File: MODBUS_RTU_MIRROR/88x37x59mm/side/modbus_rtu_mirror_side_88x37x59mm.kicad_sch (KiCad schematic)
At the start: 5 parts, among them J1 Conn_01x04_Male, J2 Conn_01x04_Male, U1 ESP32-WROOM-32, U2 TXS0108EPW, U3 AMS1117-3.3

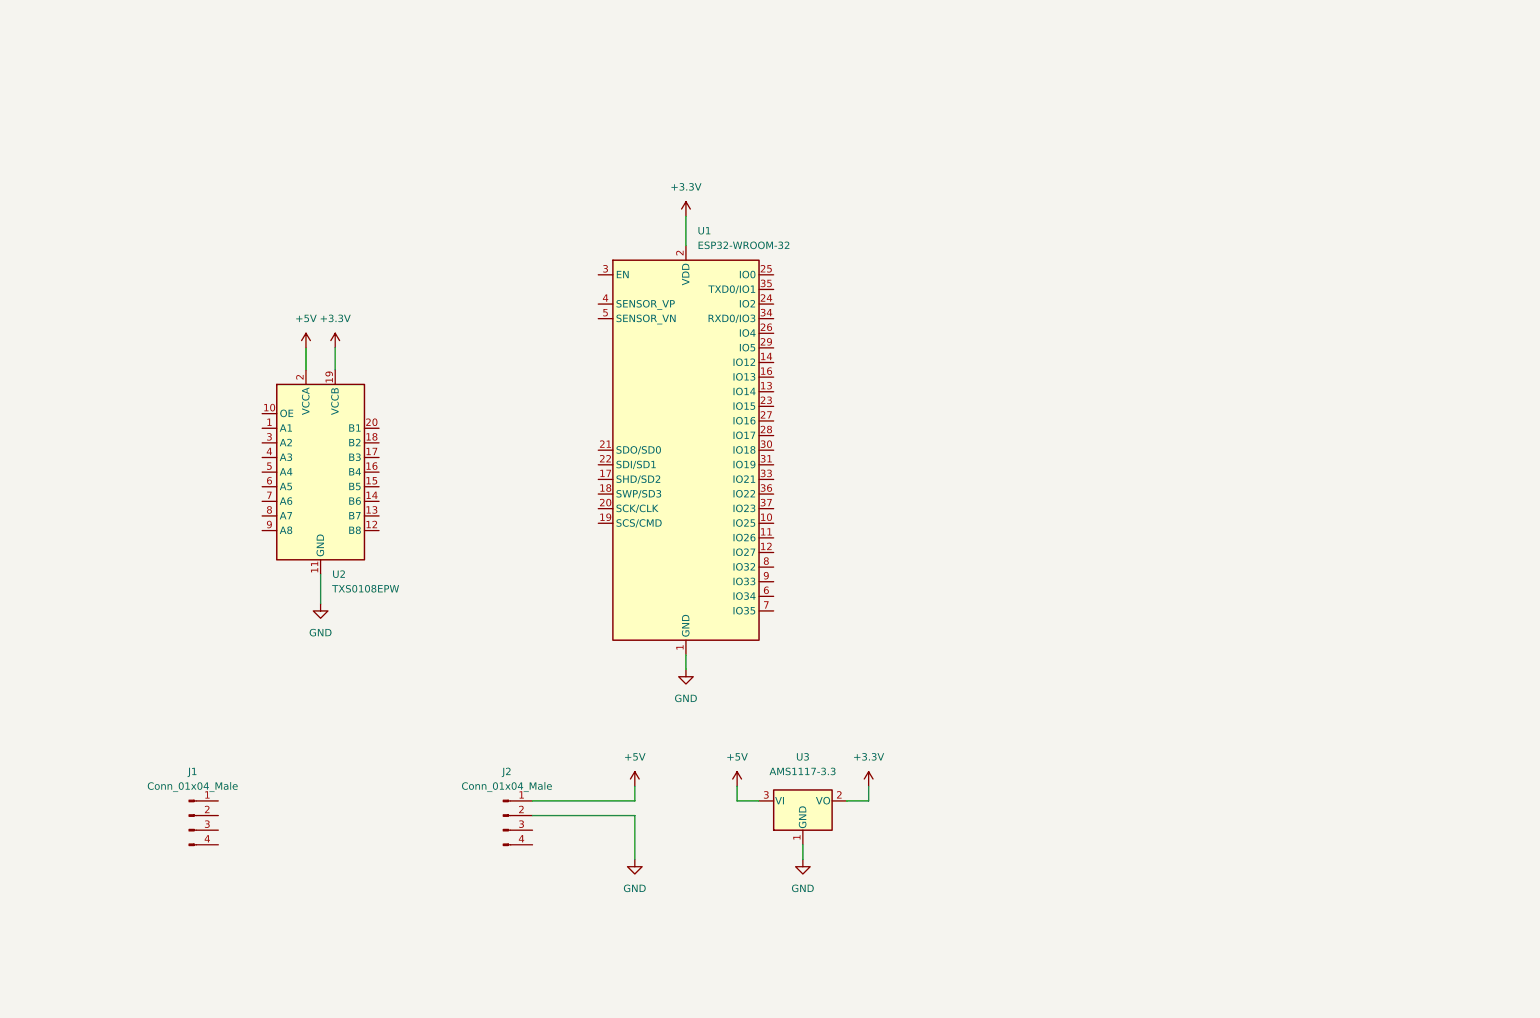
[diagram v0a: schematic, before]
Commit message: added capacitors, rtc, prog header
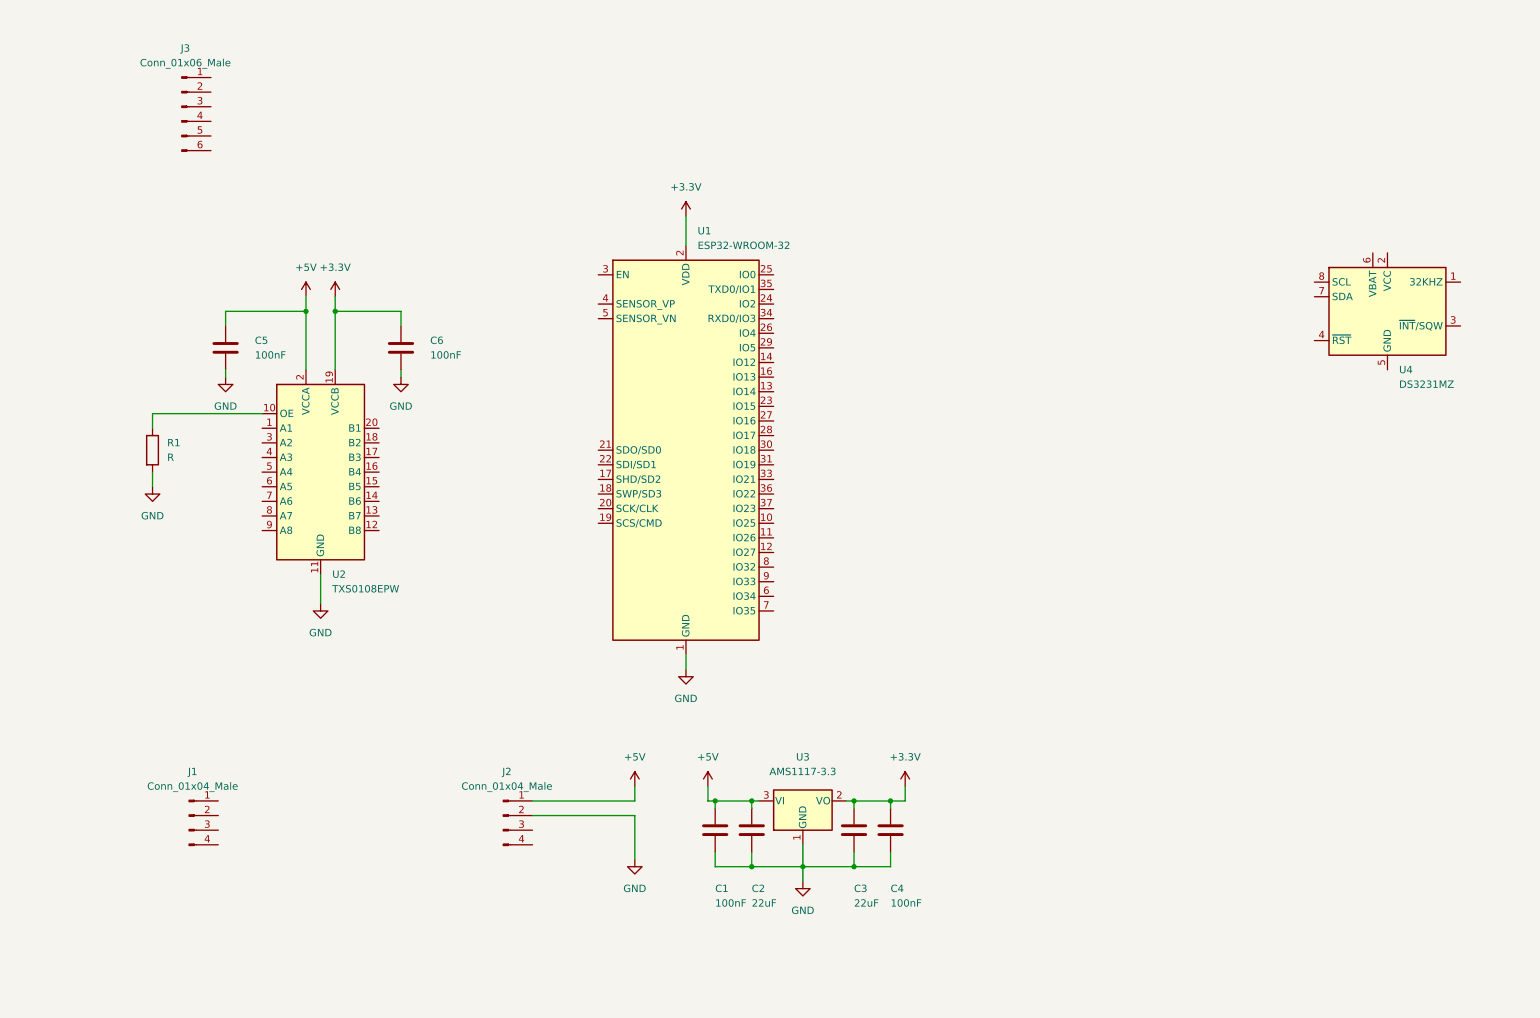
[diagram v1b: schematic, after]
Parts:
- added C1, C4, C5, C6: 100nF, Capacitor_SMD:C_0805_2012Metric_Pad1.18x1.45mm_HandSolder, symbol Device:C
- added C2, C3: 22uF, Capacitor_SMD:C_0805_2012Metric_Pad1.18x1.45mm_HandSolder, symbol Device:C
- added J3: Conn_01x06_Male, Connector_PinHeader_2.54mm:PinHeader_1x06_P2.54mm_Vertical, symbol Connector:Conn_01x06_Male
- added R1: R, Resistor_SMD:R_0805_2012Metric_Pad1.20x1.40mm_HandSolder, symbol Device:R
- added U4: DS3231MZ, Package_SO:SOIC-8_3.9x4.9mm_P1.27mm, symbol Timer_RTC:DS3231MZ
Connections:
- net +3.3V: now also C3.1, C4.1, C6.1
- net +5V: now also C1.1, C2.1, C5.1
- net GND: now also C1.2, C2.2, C3.2, C4.2, C5.2, C6.2, R1.2
- net at U2.10 (OE): now also R1.1

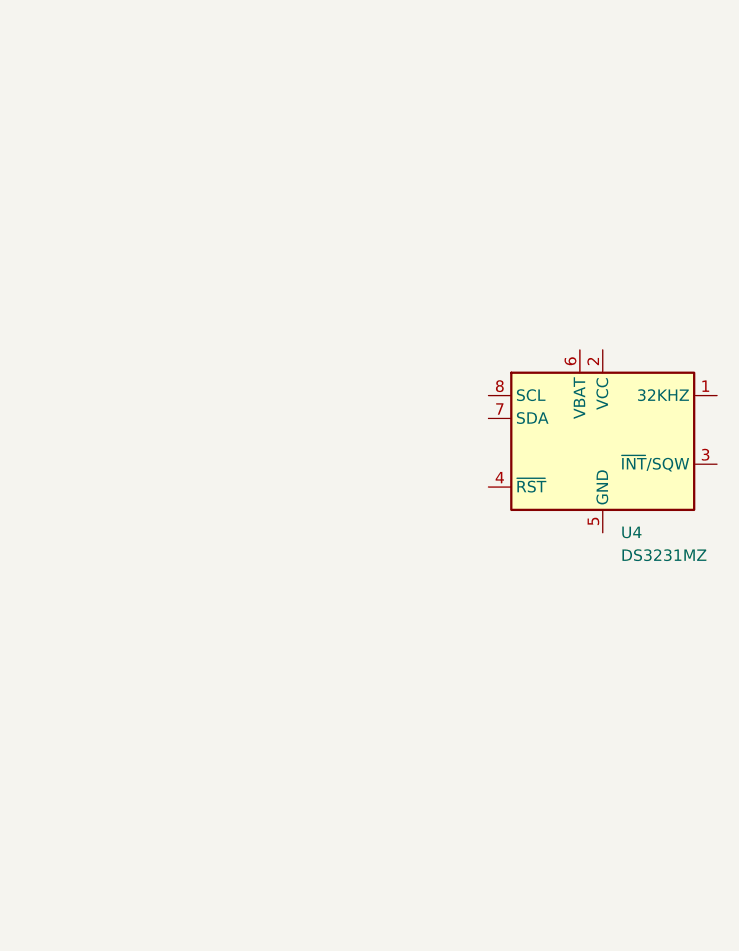
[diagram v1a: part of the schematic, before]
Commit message: added leds and pushbutton
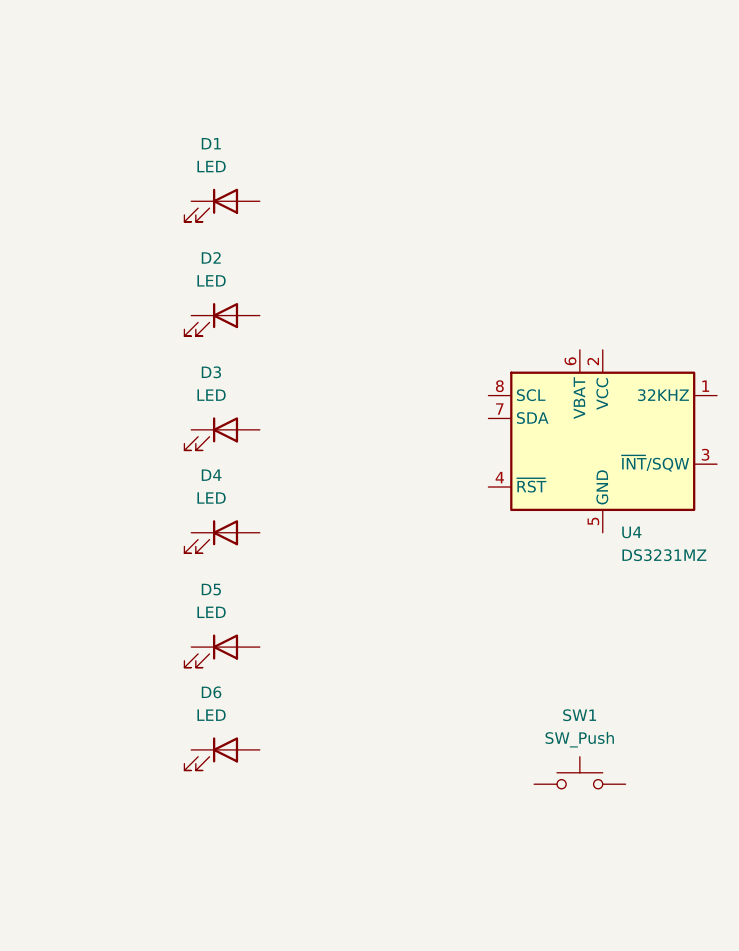
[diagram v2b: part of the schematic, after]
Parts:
- added D1, D2, D3, D4, D5, D6: LED, LED_THT:LED_D3.0mm, symbol Device:LED
- added SW1: SW_Push, Button_Switch_THT:SW_Tactile_SPST_Angled_PTS645Vx31-2LFS, symbol Switch:SW_Push
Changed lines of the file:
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@@
     (pin "1")
+  )
+  (symbol (lib_id "Device:LED") (at 212.09 106.68 0) (unit 1)
+    (in_bom yes) (on_board yes) (fields_autoplaced)
+    (property "Reference" "D6" (id 0) (at 210.5025 100.33 0))
+    (property "Value" "LED" (id 1) (at 210.5025 102.87 0))
+    (property "Footprint" "LED_THT:LED_D3.0mm" (id 2) (at 212.09 106.68 0)
+      (effects (font (size 1.27 1.27)) hide)
+    )
+    (property "Datasheet" "~" (id 3) (at 212.09 106.68 0)
+      (effects (font (size 1.27 1.27)) hide)
+    )
+    (pin "1")
+    (pin "2")
+  )
+  (symbol (lib_id "Device:LED") (at 212.09 82.55 0) (unit 1)
+    (in_bom yes) (on_board yes) (fields_autoplaced)
+    (property "Reference" "D4" (id 0) (at 210.5025 76.2 0))
+    (property "Value" "LED" (id 1) (at 210.5025 78.74 0))
+    (property "Footprint" "LED_THT:LED_D3.0mm" (id 2) (at 212.09 82.55 0)
+      (effects (font (size 1.27 1.27)) hide)
+    )
+    (property "Datasheet" "~" (id 3) (at 212.09 82.55 0)
+      (effects (font (size 1.27 1.27)) hide)
+    )
+    (pin "1")
+    (pin "2")
   )
   (symbol (lib_id "Device:C") (at 167.64 162.56 0) (unit 1)
@@
     )
     (property "Datasheet" "~" (id 3) (at 39.37 96.52 0)
+      (effects (font (size 1.27 1.27)) hide)
+    )
+    (pin "1")
+    (pin "2")
+  )
+  (symbol (lib_id "Switch:SW_Push") (at 251.46 110.49 0) (unit 1)
+    (in_bom yes) (on_board yes) (fields_autoplaced)
+    (property "Reference" "SW1" (id 0) (at 251.46 102.87 0))
+    (property "Value" "SW_Push" (id 1) (at 251.46 105.41 0))
+    (property "Footprint" "Button_Switch_THT:SW_Tactile_SPST_Angled_PTS645Vx31-2LFS" (id 2) (at 251.46 105.41 0)
+      (effects (font (size 1.27 1.27)) hide)
+    )
+    (property "Datasheet" "~" (id 3) (at 251.46 105.41 0)
       (effects (font (size 1.27 1.27)) hide)
     )
@@
     (pin "9")
   )
+  (symbol (lib_id "Device:LED") (at 212.09 58.42 0) (unit 1)
+    (in_bom yes) (on_board yes) (fields_autoplaced)
+    (property "Reference" "D2" (id 0) (at 210.5025 52.07 0))
+    (property "Value" "LED" (id 1) (at 210.5025 54.61 0))
+    (property "Footprint" "LED_THT:LED_D3.0mm" (id 2) (at 212.09 58.42 0)
+      (effects (font (size 1.27 1.27)) hide)
+    )
+    (property "Datasheet" "~" (id 3) (at 212.09 58.42 0)
+      (effects (font (size 1.27 1.27)) hide)
+    )
+    (pin "1")
+    (pin "2")
+  )
   (symbol (lib_id "Timer_RTC:DS3231MZ") (at 254 72.39 0) (unit 1)
     (in_bom yes) (on_board yes) (fields_autoplaced)
@@
     (pin "4")
   )
+  (symbol (lib_id "Device:LED") (at 212.09 95.25 0) (unit 1)
+    (in_bom yes) (on_board yes) (fields_autoplaced)
+    (property "Reference" "D5" (id 0) (at 210.5025 88.9 0))
+    (property "Value" "LED" (id 1) (at 210.5025 91.44 0))
+    (property "Footprint" "LED_THT:LED_D3.0mm" (id 2) (at 212.09 95.25 0)
+      (effects (font (size 1.27 1.27)) hide)
+    )
+    (property "Datasheet" "~" (id 3) (at 212.09 95.25 0)
+      (effects (font (size 1.27 1.27)) hide)
+    )
+    (pin "1")
+    (pin "2")
+  )
   (symbol (lib_id "power:GND") (at 82.55 83.82 0) (unit 1)
     (in_bom yes) (on_board yes) (fields_autoplaced)
@@
     (pin "3")
   )
+  (symbol (lib_id "Device:LED") (at 212.09 71.12 0) (unit 1)
+    (in_bom yes) (on_board yes) (fields_autoplaced)
+    (property "Reference" "D3" (id 0) (at 210.5025 64.77 0))
+    (property "Value" "LED" (id 1) (at 210.5025 67.31 0))
+    (property "Footprint" "LED_THT:LED_D3.0mm" (id 2) (at 212.09 71.12 0)
+      (effects (font (size 1.27 1.27)) hide)
+    )
+    (property "Datasheet" "~" (id 3) (at 212.09 71.12 0)
+      (effects (font (size 1.27 1.27)) hide)
+    )
+    (pin "1")
+    (pin "2")
+  )
   (symbol (lib_id "power:+3.3V") (at 132.08 55.88 0) (unit 1)
     (in_bom yes) (on_board yes) (fields_autoplaced)
@@
     )
     (pin "1")
+  )
+  (symbol (lib_id "Device:LED") (at 212.09 45.72 0) (unit 1)
+    (in_bom yes) (on_board yes) (fields_autoplaced)
+    (property "Reference" "D1" (id 0) (at 210.5025 39.37 0))
+    (property "Value" "LED" (id 1) (at 210.5025 41.91 0))
+    (property "Footprint" "LED_THT:LED_D3.0mm" (id 2) (at 212.09 45.72 0)
+      (effects (font (size 1.27 1.27)) hide)
+    )
+    (property "Datasheet" "~" (id 3) (at 212.09 45.72 0)
+      (effects (font (size 1.27 1.27)) hide)
+    )
+    (pin "1")
+    (pin "2")
   )
   (symbol (lib_id "RF_Module:ESP32-WROOM-32") (at 132.08 96.52 0) (unit 1)
@@
       (reference "C6") (unit 1) (value "100nF") (footprint "Capacitor_SMD:C_0805_2012Metric_Pad1.18x1.45mm_HandSolder")
     )
+    (path "/dc7af683-2c85-4d4e-8d40-70498e51a028"
+      (reference "D1") (unit 1) (value "LED") (footprint "LED_THT:LED_D3.0mm")
+    )
+    (path "/5f47507c-41a1-4dac-9fb1-1387dec1beee"
+      (reference "D2") (unit 1) (value "LED") (footprint "LED_THT:LED_D3.0mm")
+    )
+    (path "/c32448ac-696d-4e56-8fe3-70af80bdc8e7"
+      (reference "D3") (unit 1) (value "LED") (footprint "LED_THT:LED_D3.0mm")
+    )
+    (path "/30cbad51-0cb1-40e1-9046-3e01b9d29e56"
+      (reference "D4") (unit 1) (value "LED") (footprint "LED_THT:LED_D3.0mm")
+    )
+    (path "/764aed26-a6fd-48d9-8155-e9d3012cf868"
+      (reference "D5") (unit 1) (value "LED") (footprint "LED_THT:LED_D3.0mm")
+    )
+    (path "/2c7eb952-1cb1-4d80-b65b-37a12e2d3fdc"
+      (reference "D6") (unit 1) (value "LED") (footprint "LED_THT:LED_D3.0mm")
+    )
     (path "/49c63bb9-4dc7-4ee9-a008-aa76eab3ac51"
       (reference "J1") (unit 1) (value "Conn_01x04_Male") (footprint "Connector_PinHeader_2.54mm:PinHeader_1x04_P2.54mm_Vertical")
@@
       (reference "R1") (unit 1) (value "R") (footprint "Resistor_SMD:R_0805_2012Metric_Pad1.20x1.40mm_HandSolder")
     )
+    (path "/4588914e-a739-4fa5-a786-669b024e5930"
+      (reference "SW1") (unit 1) (value "SW_Push") (footprint "Button_Switch_THT:SW_Tactile_SPST_Angled_PTS645Vx31-2LFS")
+    )
     (path "/fb0c2f3f-6546-40cd-8df4-7425a33df075"

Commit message: added vertical CR2032 connector
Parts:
- added BT1: Battery_Cell, Battery_rtc:CR2032_Vertical_CircularHoles, symbol Device:Battery_Cell
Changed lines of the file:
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@@
+    (pin "2")
+  )
+  (symbol (lib_id "Device:Battery_Cell") (at 254 43.18 0) (unit 1)
+    (in_bom yes) (on_board yes) (fields_autoplaced)
+    (property "Reference" "BT1" (id 0) (at 257.81 39.8779 0)
+      (effects (font (size 1.27 1.27)) (justify left))
+    )
+    (property "Value" "Battery_Cell" (id 1) (at 257.81 42.4179 0)
+      (effects (font (size 1.27 1.27)) (justify left))
+    )
+    (property "Footprint" "Battery_rtc:CR2032_Vertical_CircularHoles" (id 2) (at 254 41.656 90)
+      (effects (font (size 1.27 1.27)) hide)
+    )
+    (property "Datasheet" "~" (id 3) (at 254 41.656 90)
+      (effects (font (size 1.27 1.27)) hide)
+    )
+    (pin "1")
     (pin "2")
   )
@@
       (reference "#PWR0113") (unit 1) (value "GND") (footprint "")
     )
+    (path "/327edd8b-23a3-47a1-9839-5e3ee5692121"
+      (reference "BT1") (unit 1) (value "Battery_Cell") (footprint "Battery_rtc:CR2032_Vertical_CircularHoles")
+    )
     (path "/0edc8ca7-7aca-47dd-bd80-a22262ceb286"

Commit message: all elements placed
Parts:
- added C7, C8, C9: 100nF, Capacitor_SMD:C_0805_2012Metric_Pad1.18x1.45mm_HandSolder, symbol Device:C
- added R10: NONE, Resistor_SMD:R_0805_2012Metric_Pad1.20x1.40mm_HandSolder, symbol Device:R
- added R11, R8: 10k, Resistor_SMD:R_0805_2012Metric_Pad1.20x1.40mm_HandSolder, symbol Device:R
- added R12, R13: 4.7k, Resistor_SMD:R_0805_2012Metric_Pad1.20x1.40mm_HandSolder, symbol Device:R
- added R2, R3, R4, R5, R6, R7: 1k, Resistor_SMD:R_0805_2012Metric_Pad1.20x1.40mm_HandSolder, symbol Device:R
- added R9: 0, Resistor_SMD:R_0805_2012Metric_Pad1.20x1.40mm_HandSolder, symbol Device:R
- added U5: FM24C64C, Package_SO:SOIC-8_3.9x4.9mm_P1.27mm, symbol Memory_NVRAM:FM24C64C
- R1: value R -> 0
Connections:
- net +3.3V: now also D1.2 (A), D3.2 (A), D4.2 (A), D5.2 (A), D6.2 (A), J3.4 (Pin_4), R1.1, U2.2 (VCCA), U4.2 (VCC), C8.1, C9.1, R11.1, R12.1, R13.1, R8.1, U5.8 (VDD); no longer U2.19 (VCCB)
- net +5V: now also U2.19 (VCCB); no longer U2.2 (VCCA)
- net GND: now also BT1.2 (-), J3.1 (Pin_1), SW1.2, U4.5 (GND), C7.2, C8.2, C9.2, R2.1, R3.1, R9.2, U5.1 (A0), U5.2 (A1), U5.3 (A2), U5.4 (VSS), U5.7 (WP); no longer R1.2
- net ESP_TXD: now reaches J3.2 (Pin_2)
- net ESP_TXD: now also U1.35 (TXD0/IO1)
- net ESP_RXD: now reaches J3.3 (Pin_3)
- net ESP_RXD: now also U1.34 (RXD0/IO3)
- net ESP_EN: now reaches J3.5 (Pin_5)
- net ESP_EN: now also U1.3 (EN), C7.1, R11.2
- net ESP_IO0: now reaches J3.6 (Pin_6)
- net ESP_IO0: now also U1.25 (IO0)
- net at D6.1 (K): now also R7.2
- net at D4.1 (K): now also R5.2
- net +BATT: now reaches BT1.1 (+)
- net +BATT: now also U4.6 (VBAT)
- net at U2.10 (OE): now also R1.2; no longer R1.1
- net STP_SW: now reaches SW1.1
- net STP_SW: now also U1.12 (IO27), R8.2
- net at J1.1 (Pin_1): now also U2.17 (B3)
- net at J1.2 (Pin_2): now also U2.16 (B4)
- net at J1.3 (Pin_3): now also U2.15 (B5)
- net at J1.4 (Pin_4): now also U2.14 (B6)
- net RX2_LED: now reaches U2.1 (A1)
- net RX2_LED: now also U1.26 (IO4), R5.1
- net at U2.18 (B2): now also J2.4 (Pin_4)
- net at U2.20 (B1): now also J2.3 (Pin_3)
- net at U2.3 (A2): now also R10.1, R9.1
- net TX2_LED: now reaches U2.4 (A3)
- net TX2_LED: now also U1.28 (IO17), R4.1
- net RX1_LED: now reaches U2.5 (A4)
- net RX1_LED: now also U1.30 (IO18), R7.1
- net at U2.6 (A5): now also U1.31 (IO19)
- net TX1_LED: now reaches U2.7 (A6)
- net TX1_LED: now also U1.33 (IO21), R6.1
- net at D2.1 (K): now also R3.2
- net STP_LED: now reaches D2.2 (A)
- net STP_LED: now also U1.37 (IO23)
- net I2C0_SDA: now reaches U4.7 (SDA)
- net I2C0_SDA: now also U1.8 (IO32), R12.2, U5.5 (SDA)
- net I2C0_SCL: now reaches U4.8 (SCL)
- net I2C0_SCL: now also U1.9 (IO33), R13.2, U5.6 (SCL)
- net at D5.1 (K): now also R6.2
- net at D3.1 (K): now also R4.2
- net at D1.1 (K): now also R2.2
- net at U1.27 (IO16): now also R10.2
- no-connect marks 0 -> 26
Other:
- note added: "+5V"
- note added: "3.3V I2C FRAM"
- note added: "EN1"
- note added: "EN2"
- note added: "GND"
- note added: "POWER"
- note added: "Programming header"
- note added: "R9=0,R10=NONE. RX2 ONLY INPUT (FAILSAFE) R9=NONE,R10=0. RX2/TX2 BIDIRECTIONAL MCU CONTROLLED"
- note added: "RTC Battery"
- note added: "RX1"
- note added: "RX2"
- note added: "RX_1"
- note added: "RX_2"
- note added: "SETUP"
- note added: "TO BASE BOARD"
- note added: "TX1"
- note added: "TX2"
- note added: "TX_1"
- note added: "TX_2"
- moved on the sheet: BT1, C1, C2, C3, C4, D1, D2, D3, D4, D5, D6, J1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
